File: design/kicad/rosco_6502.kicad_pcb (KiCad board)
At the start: 4 copper layers, 100 x 100 mm, 60 parts, among them IC1 W65C02SxP, IC2 ATF22V10C-7PX, IC3 XR68C681CJTR-F, IC4 NE555P, IC5 ATF22V10C-7PX, J1 UART_A, J2 UART_B, J3 Conn_01x06, J4 Conn_01x01_Male, J5 Conn_02x18_Odd_Even, J6 Conn_01x02_Male, J7 Jack-DC, Q1 3.6864MHz, U1 AS6C4008-55PCN, U2 AS6C62256-55PCN, U3 AT28C64B-15PU, U4 74HCT174, X1 14MHz

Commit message: Bank ROM
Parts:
- U3: value AT28C64B-15PU -> AT28C256-15PU; footprint Package_DIP:DIP-28_W15.24mm_Socket_LongPads -> Package_DIP:DIP-28_W15.24mm
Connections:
- U3 pad 1: unconnected-(U3-Pad1) -> BANK5
- U3 pad 26: unconnected-(U3-Pad26) -> BANK4
- U4 pad 12: unconnected-(U4-Pad12) -> BANK5
- U4 pad 13: GND -> D5
- U4 pad 14: GND -> D4
- U4 pad 15: unconnected-(U4-Pad15) -> BANK4
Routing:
- net BANK5: track 0.00 -> 102.4 mm, vias 0 -> 2
- net BANK4: track 0.00 -> 75.0 mm, vias 0 -> 2
- net D5: track 131.9 -> 179.1 mm, vias 1 -> 2
- net D4: track 129.2 -> 170.9 mm, vias 1 -> 2
- net ~{VP}: track 182.1 -> 179.0 mm
- net ~{ML}: track 156.2 -> 158.4 mm
- net NMI: track 224.4 -> 225.8 mm
- net D1: track 198.2 -> 197.3 mm
- net R/~{W}: track 269.7 -> 269.1 mm
- net IRQ: track 216.8 -> 217.3 mm
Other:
- board text added: "AS6C4008"
- board text added: "AS6C62256"
- board text added: "AT28C64B ~or~ AT28C256"
- board text added: "Copyright (c)2022-2023 Ross Bamford & Contributors"
- board text added: "r4"
- board text removed: "Copyright (c)2022 Ross Bamford & Contributors"
- board text removed: "r3"

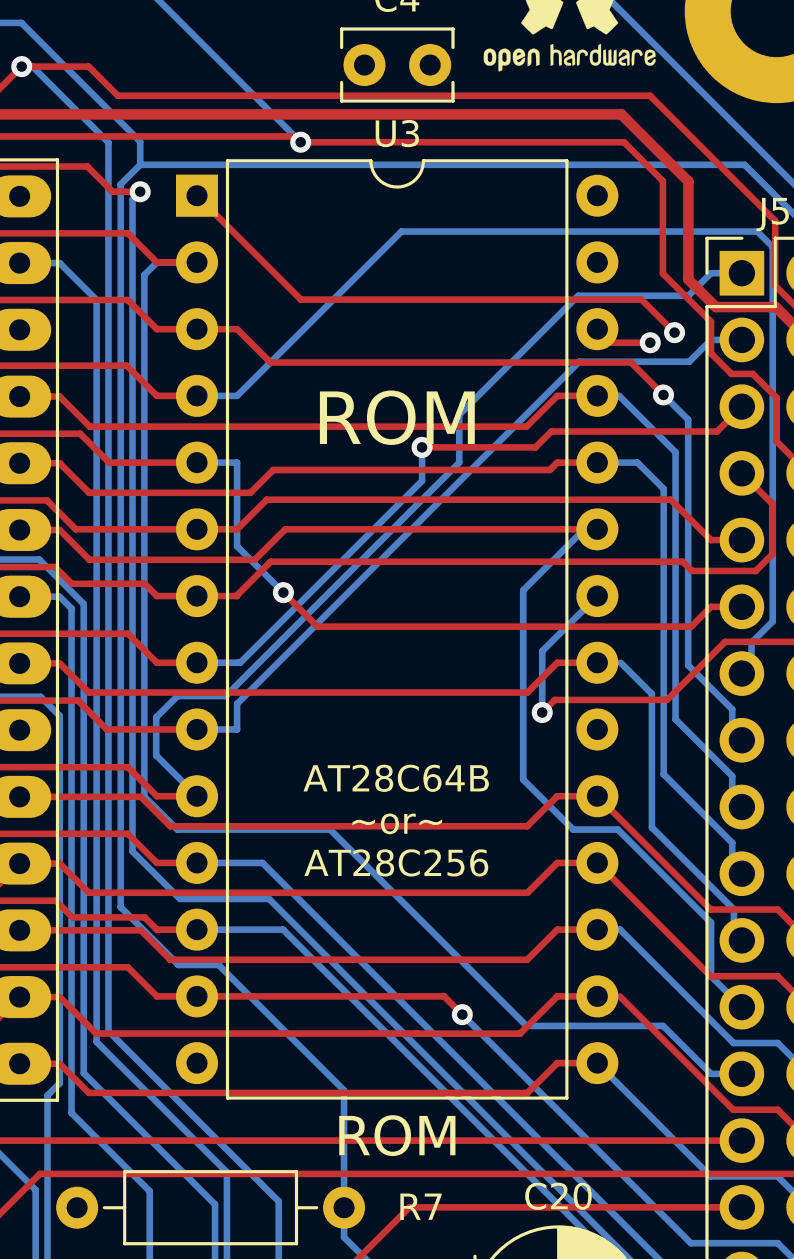
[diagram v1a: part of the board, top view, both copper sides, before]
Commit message: Fix ROM footprint; README
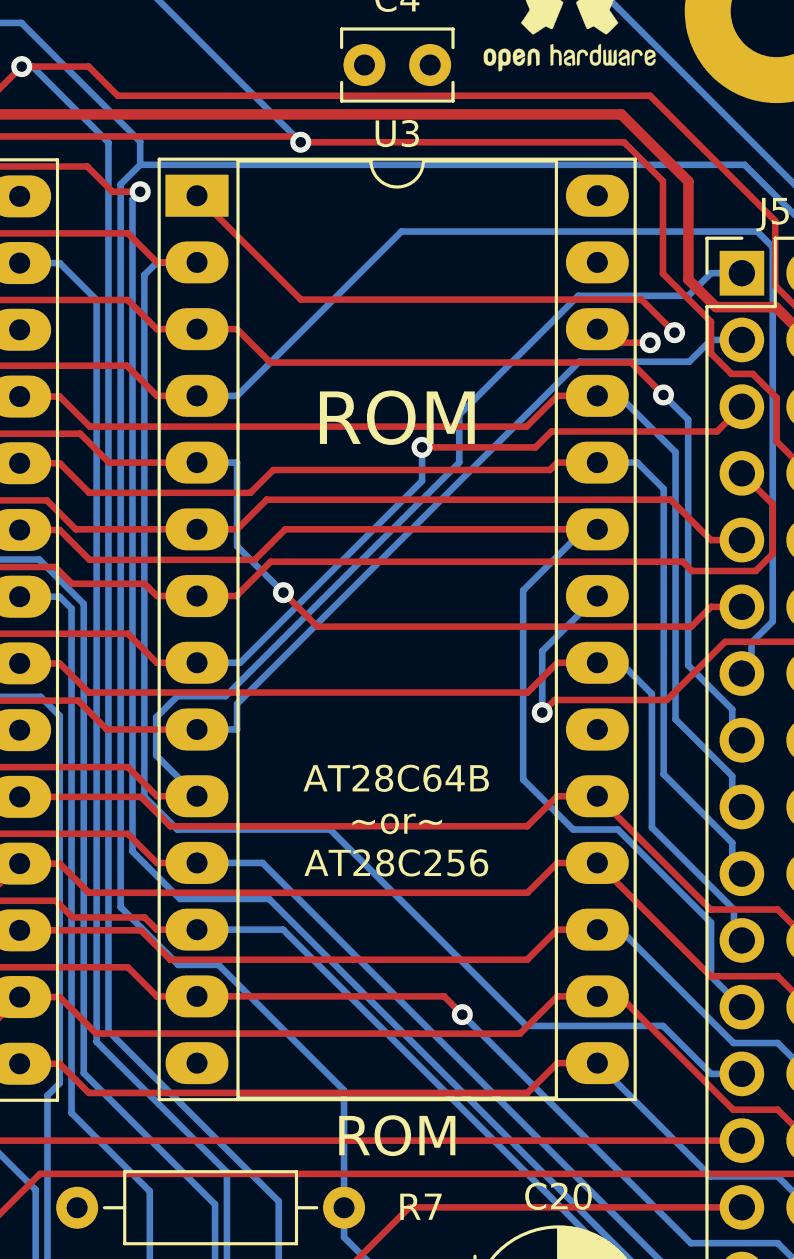
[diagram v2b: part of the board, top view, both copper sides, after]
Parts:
- U3: footprint Package_DIP:DIP-28_W15.24mm -> Package_DIP:DIP-28_W15.24mm_Socket_LongPads
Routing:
- net D5: track 179.1 -> 178.2 mm
- net A8: track 183.9 -> 183.1 mm
- net BANK4: track 75.0 -> 74.3 mm

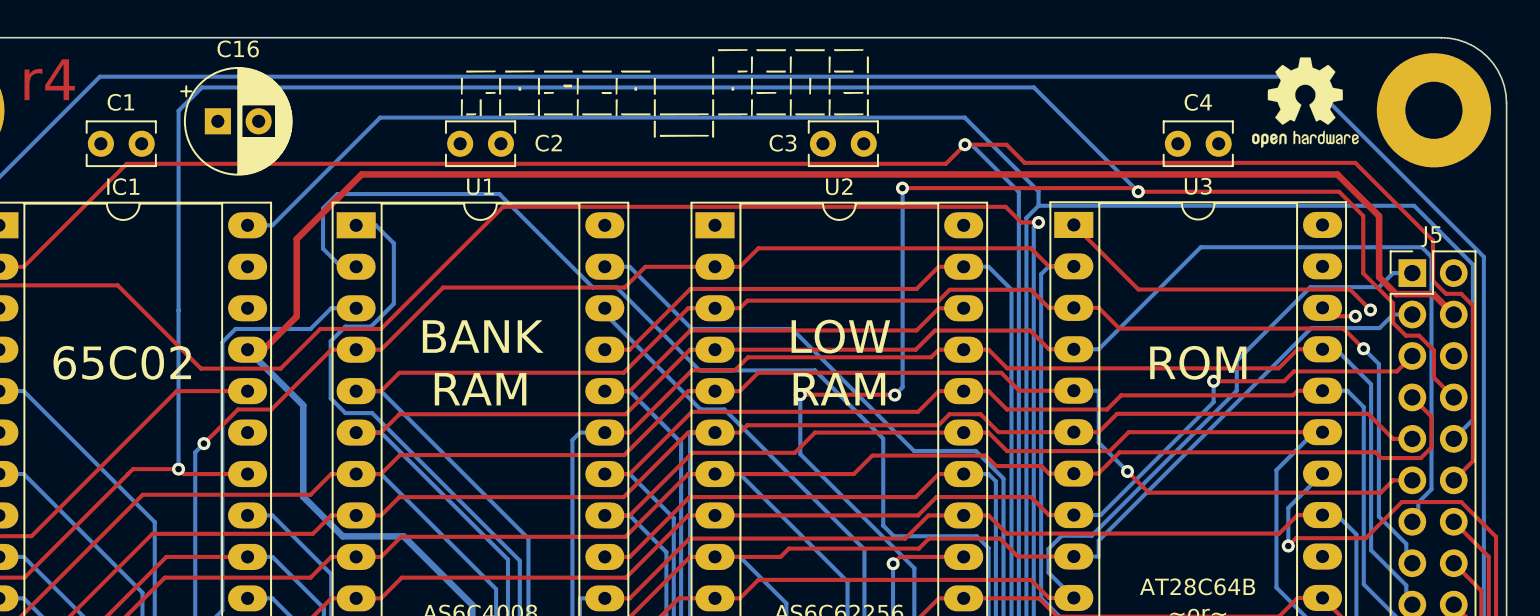
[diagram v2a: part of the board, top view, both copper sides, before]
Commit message: Support other ROM as discussed https://discord.com/channels/698525682199822367/1004479727786012803/1005127547442429995
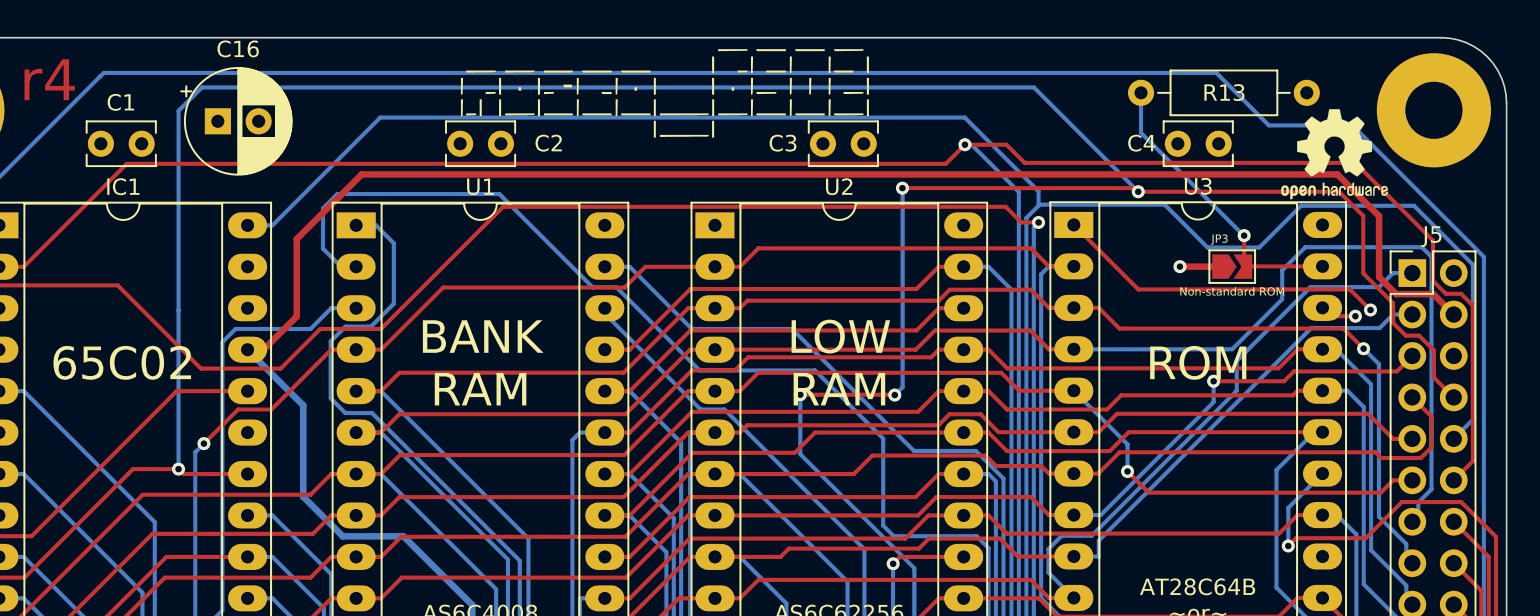
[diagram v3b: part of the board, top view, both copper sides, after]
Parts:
- added JP3: SolderJumper_2_Open, Jumper:SolderJumper-2_P1.3mm_Open_TrianglePad1.0x1.5mm, F.Cu at (167.2, 63.0)
- added R13: 3K3, Resistor_THT:R_Axial_DIN0207_L6.3mm_D2.5mm_P10.16mm_Horizontal, F.Cu at (161.6, 52.4)
- moved ohw 3.64 mm to (173.5, 56.1)
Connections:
- U3 pad 27: VCC -> Net-(U3-Pad27)
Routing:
- net Net-(U3-Pad27): track 0.00 -> 18.1 mm, vias 0 -> 1
- net GND: track 32.8 -> 35.2 mm, vias 0 -> 1
- net ~{RESET}: track 238.8 -> 241.0 mm
- net A6: track 204.2 -> 205.3 mm
- net A5: track 189.4 -> 188.5 mm
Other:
- board text added: "(c)2022-2023 Ross Bamford & Contributors"
- board text added: "Non-standard ROM"
- board text removed: "Copyright (c)2022-2023 Ross Bamford & Contributors"

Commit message: Update for Kicad 7
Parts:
- IC4: footprint Package_DIP:DIP-8_W7.62mm_Socket_LongPads -> Package_DIP:DIP-8_W7.62mm
- J6: value Conn_01x02_Male -> Conn_01x02_Pin

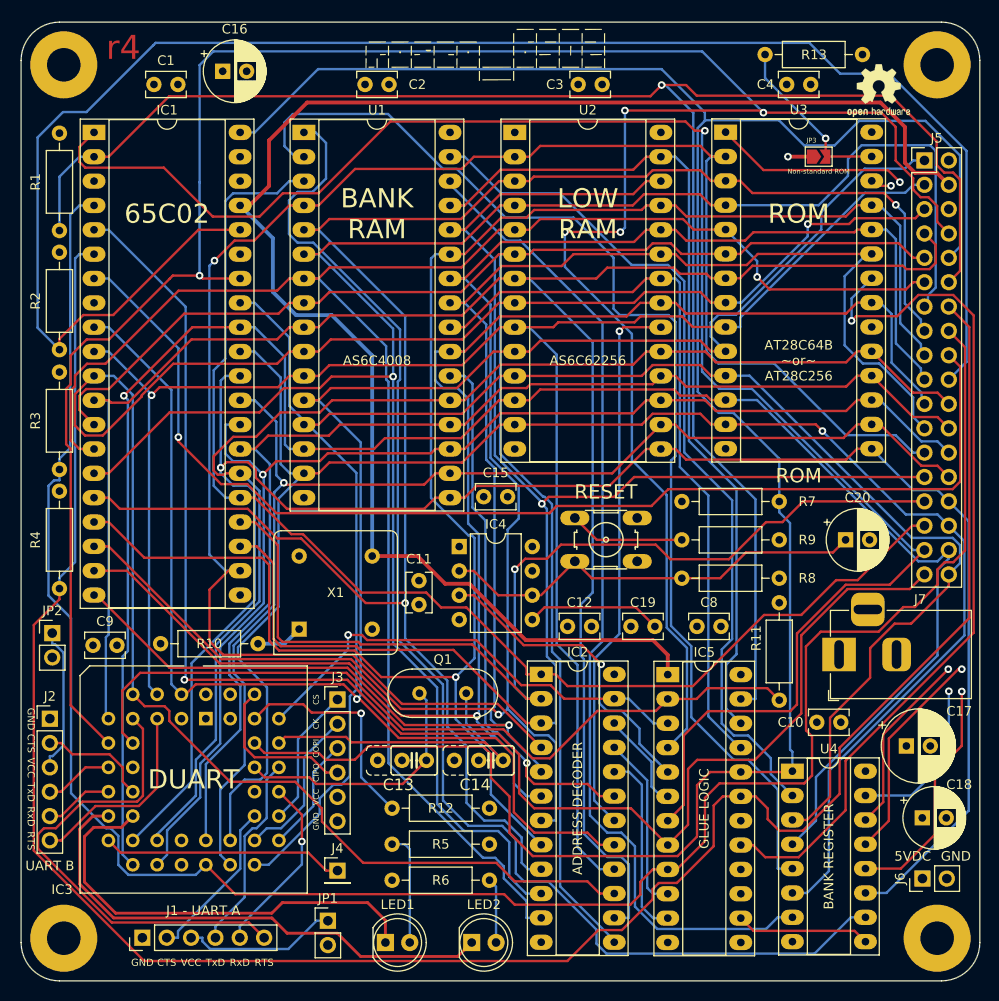
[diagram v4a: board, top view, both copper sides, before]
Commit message: Switch ROM to SST39SF010
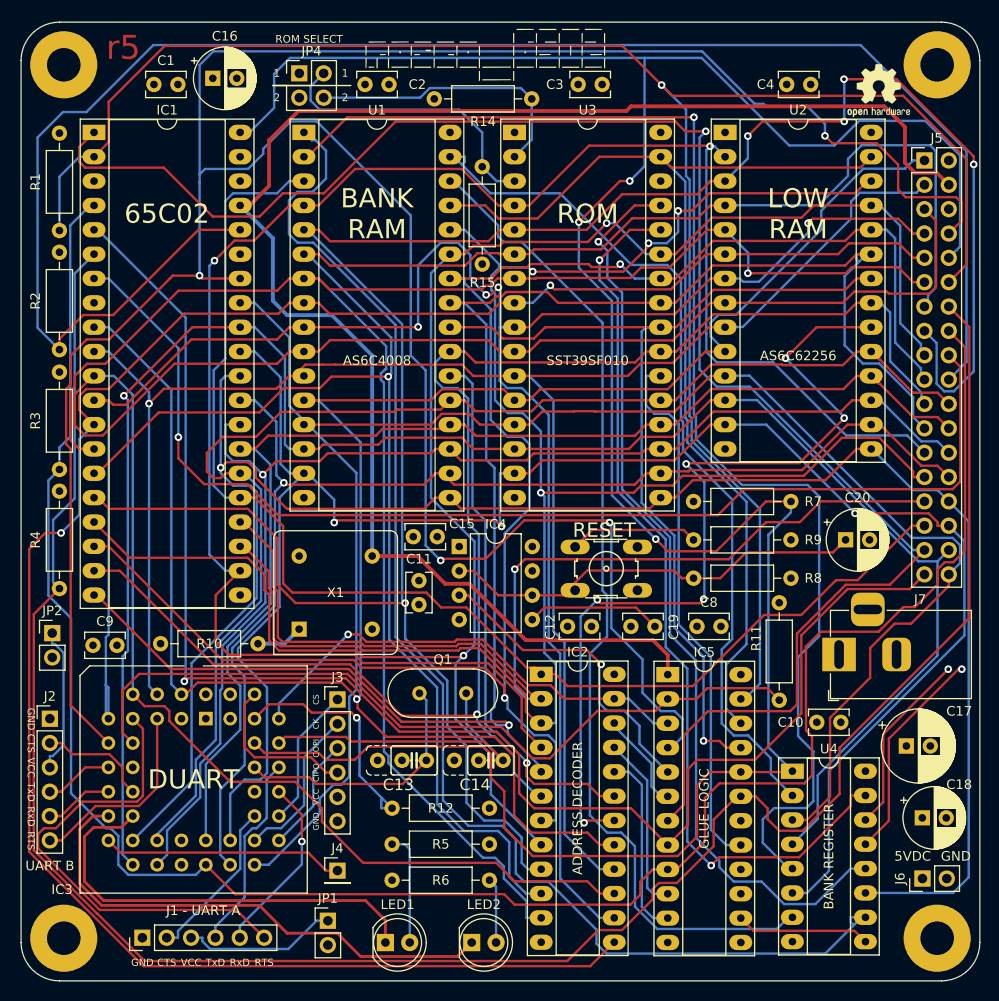
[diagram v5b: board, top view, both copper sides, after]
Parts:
- removed JP3: SolderJumper_2_Open, Jumper:SolderJumper-2_P1.3mm_Open_TrianglePad1.0x1.5mm
- removed R13: 3K3, Resistor_THT:R_Axial_DIN0207_L6.3mm_D2.5mm_P10.16mm_Horizontal
- added JP4: Conn_02x02_Odd_Even, Connector_PinHeader_2.54mm:PinHeader_2x02_P2.54mm_Vertical, F.Cu at (113.0, 54.3)
- added R14: 3K3, Resistor_THT:R_Axial_DIN0207_L6.3mm_D2.5mm_P10.16mm_Horizontal, F.Cu at (137.3, 57.0)
- added R15: 3K3, Resistor_THT:R_Axial_DIN0207_L6.3mm_D2.5mm_P10.16mm_Horizontal, F.Cu at (132.1, 64.1)
- U3: value AT28C256-15PU -> SST39SF010; footprint Package_DIP:DIP-28_W15.24mm_Socket_LongPads -> Package_DIP:DIP-32_W15.24mm_Socket_LongPads
- moved U3 22.0 mm to (135.5, 60.5)
- moved U2 21.9 mm to (157.4, 60.5)
- moved C15 8.44 mm to (124.9, 102.7)
- moved S1 3.02 mm to (145.0, 106.0)
- moved C16 1.26 mm to (104.0, 54.9)
- moved R7 1.22 mm to (154.1, 99.0)
- moved R8 1.22 mm to (154.1, 107.0)
- moved R9 1.22 mm to (154.1, 103.0)
- renumbered REF** to PARITY, REF** to ROHS
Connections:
- U3 pad 1: BANK5 -> unconnected-(U3-NC-Pad1)
- U3 pad 10: A0 -> A2
- U3 pad 11: D0 -> A1
- U3 pad 12: D1 -> A0
- U3 pad 13: D2 -> D0
- U3 pad 14: GND -> D1
- U3 pad 15: D3 -> D2
- U3 pad 16: D4 -> GND
- U3 pad 17: D5 -> D3
- U3 pad 18: D6 -> D4
- U3 pad 19: D7 -> D5
- U3 pad 2: A12 -> Net-(JP4-Pin_4)
- U3 pad 20: GND -> D6
- U3 pad 21: A10 -> D7
- U3 pad 23: A11 -> A10
- U3 pad 24: A9 -> ~{RD}
- U3 pad 25: A8 -> A11
- U3 pad 26: BANK4 -> A9
- U3 pad 27: Net-(JP3-B) -> A8
- U3 pad 28: VCC -> BANK4
- U3 pad 3: A7 -> Net-(JP4-Pin_2)
- U3 pad 4: A6 -> A12
- U3 pad 5: A5 -> A7
- U3 pad 6: A4 -> A6
- U3 pad 7: A3 -> A5
- U3 pad 8: A2 -> A4
- U3 pad 9: A1 -> A3
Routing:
- net A7: track 195.8 -> 234.9 mm, vias 2 -> 5
- net A4: track 177.7 -> 215.6 mm, vias 0 -> 2
- net ~{ROMOE}: track 90.7 -> 56.3 mm, vias 1 -> 0
- net ~{LOWRAM}: track 57.5 -> 91.2 mm, vias 1 -> 6
- net ~{RESET}: track 241.0 -> 273.2 mm, vias 0 -> 3
- net Net-(JP4-Pin_2): track 0.00 -> 30.2 mm
- net Net-(JP4-Pin_4): track 0.00 -> 29.4 mm
- net ~{WR}: track 87.7 -> 112.4 mm
- net A13: track 167.3 -> 191.7 mm, vias 1 -> 4
- net R/~{W}: track 269.1 -> 291.7 mm, vias 5 -> 4
- net ~{RD}: track 76.6 -> 98.7 mm, vias 0 -> 1
- net BANK4: track 74.3 -> 95.4 mm
- net Net-(JP3-B): track 18.1 -> 0.00 mm, vias 1 -> 0
- net BANK1: track 121.5 -> 136.6 mm, vias 0 -> 1
- net D2: track 183.4 -> 191.9 mm, vias 1 -> 3
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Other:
- board text added: "1"
- board text added: "2"
- board text added: "ROM SELECT"
- board text added: "SST39SF010"
- board text added: "r5"
- board text removed: "AT28C64B ~or~ AT28C256"
- board text removed: "Non-standard ROM"
- board text removed: "r4"
